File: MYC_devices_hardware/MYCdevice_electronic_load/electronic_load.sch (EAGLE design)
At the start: 129 parts, among them IC1 MEGA16-P, IC10 Gate7, IC11 LF347N, IC12 LF347N, IC14 MCP603CH, IC15 MCP603CH, IC16 MCP603CH, IC17 MCP603CH, IC18 MCP603CH, IC19 MCP603CH, IC2 MAX232, IC20 MCP603CH, IC3 7805TV, IC4 Gate1, IC5 Gate2, IC6 Gate3, IC7 Gate4, IC8 Gate5, IC9 Gate6, Q1 20MHz, X1 8-15V, X2 1503_09, X3 1503_09, X4 RS232

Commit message: deleted duplicate MYCdevice_electronic_load
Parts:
- removed C29, C30, C31, C32, C33: 22uF 1210, rcl:C-EUC1206
- removed R52, R57: 27k, resistor:R-EU_0207/2V
- removed R53, R58: 1k 1%, resistor:R-EU_0207/2V
- removed R54: 9k53, resistor:R-EU_0207/2V
- removed R55, R60: 22k, resistor:R-EU_0207/2V
- removed R56: 9k1 1%, resistor:R-EU_0207/2V
- removed R59: 9k52, resistor:R-EU_0207/2V
- removed SL7: U/Iin, con-amp-quick:M05
- added IC13: 78L5, v-reg:78LXX
- added R18, R20: 154k, resistor:R-EU_0207/2V
- added R19, R21: 18k, resistor:R-EU_0207/2V
- added T1: BC807, transistor:BC807-16-PNP-SOT23-BEC
- added T2: BC817, transistor:BC817-16-NPN-SOT23-BEC
- C10, C9: value 22u 1210 -> 22uF 1210
- C11, C12, C13, C14, C15, C16, C17, C18, C19, C20, C21, C22, C23, C24, C25: value 22u -> 22uF 1210; device resistor:C-EUC1206 -> rcl:C-EUC1206
- C2, C3: value 22uF 1210 -> 18pF; device rcl:C-EUC1206 -> resistor:C-EU025-025X050
- C28: value 22uF 1210 -> 1u; device rcl:C-EUC1206 -> resistor:C-EUC1206
- C4: value 18pF -> 22uF 1210; device resistor:C-EU025-025X050 -> rcl:C-EUC1206
- C5: value 18pF -> 22u 1210; device resistor:C-EU025-025X050 -> rcl:C-EUC1206
- C6: value 22uF 1210 -> 22u 1210
- IC10: value Gate7 -> MCP4921
- IC11, IC12: value LF347N -> LM324N; device linear:LF347N -> linear:LM324N
- IC3: value 7805TV -> 79L09; device linear:7805TV -> v-reg:78LXX
- IC4: value Gate1 -> MCP4921
- IC5: value Gate2 -> MCP4921
- IC6: value Gate3 -> MCP4921
- IC7: value Gate4 -> MCP4921
- IC8: value Gate5 -> MCP4921
- IC9: value Gate6 -> MCP4921
- L1: value (none) -> 22u
- R10, R12, R14, R16, R4, R6, R8: value 10k -> 12k
- R11, R13, R15, R17, R5, R7, R9: value 10k -> 8k2
- R22: value 68k 1% -> 154k
- R23: value na -> 18k
- R24: value 9k1 1% -> 154k
- R25: value 27k -> 18k
- R26, R38, R48: value 1k 1% -> 154k
- R27, R39, R49: value 9k53 -> 18k
- R28: value 1,8 1% -> 1k5; device resistor:R-EU_0207/2V -> resistor:R-EU_R1206
- R29: value 220k -> 180; device resistor:R-EU_0207/2V -> resistor:R-EU_R1206
- R30, R40, R50: value 22k -> 154k
- R31, R41, R46, R51: value 9k1 1% -> 18k
- R32, R42, R47: value 27k -> 154k
- R33, R43: value 1k 1% -> 18k
- R34: value 9k53 -> 8k2; device resistor:R-EU_0207/2V -> resistor:R-EU_R1206
- R35: value 22k -> 18k; device resistor:R-EU_0207/2V -> resistor:R-EU_R1206
- R36: value 9k1 1% -> 10k; device resistor:R-EU_0207/2V -> resistor:R-EU_R1206
- R37: value 27k -> 10k; device resistor:R-EU_0207/2V -> resistor:R-EU_R1206
- R44: value 9k53 -> 154k
- R45: value 22k -> 18k
- SL1: value Gates -> Gates1
- SL2: value Gates -> Gates2
- SL4, SL5: value U/Iin -> Iin
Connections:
- net N$29 renamed FET5
- removed net N$57 (its old number): C25.1, R53.2, R54.2, SL7.1
- removed net N$75: IC15.+IN, R35.1
- removed net N$77: IC16.-IN, R36.2, R37.2, R38.1, R39.1
- removed net N$78: C17.1, R40.2, SL5.3
- removed net N$83: IC11A.+IN, IC4A.VOUT
- removed net N$84: IC19.-IN, R51.2, R52.2, R53.1, R54.1
- removed net N$85: IC19.+IN, R55.1
- removed net N$86: C24.1, R55.2, SL7.2
- removed net N$87: IC20.-IN, R56.2, R57.2, R58.1, R59.1
- removed net N$88: C22.1, R60.2, SL7.4
- removed net N$92: IC11A.OUT, R4.2, SL1.1
- removed net N$93: IC10A.VOUT, IC12D.+IN
- removed net N$94: IC12D.-IN, R16.1, R17.1
- removed net N$95: IC12D.OUT, R16.2, SL2.3
- new net 9V: C27.1, IC13.IN, IC3.OUT, R34.1
- new net FET1: IC12C.OUT, R16.2, SL2.3
- new net FET2: IC12A.OUT, R12.2, SL2.2
- new net FET3: IC12D.OUT, R14.2, SL2.1
- new net FET4: IC11B.OUT, R6.2, SL1.4
- new net FET6: IC11A.OUT, R4.2, SL1.2
- new net FET7: IC11D.OUT, R10.2, SL1.1
- new net GON: IC1.(OC1A)PD5, R36.1
- new net N$27: R29.2, SL6.5
- new net N$29: R21.2, SL4.4
- new net N$32: IC20.-IN, R32.1, R33.1
- new net N$39: IC10A.VOUT, R17.2
- new net N$41: IC16.-IN, R22.1, R23.1
- new net N$45: IC17.-IN, R24.1, R25.1
- new net N$52: R48.1, SL6.1
- new net N$53: R31.2, SL6.2
- new net N$55: IC5A.VOUT, R7.2
- new net N$64: R36.2, T2.B
- new net N$65: R38.1, SL4.1
- new net N$72: IC18.+IN, R46.1, R47.2
- new net VREF: IC11A.+IN, IC11B.+IN, IC11C.+IN, IC11D.+IN, IC12A.+IN, IC12C.+IN, IC12D.+IN, R34.2, R35.1
- net C13: now also C5.1; no longer C7.1
- net GND: now also C1.1, C10.2, C2.1, C4.2, C8.1, C9.2, IC12B.+IN, IC13.GND, IC14.!CS, IC15.!CS, IC16.!CS, IC17.!CS, IC18.!CS, IC19.!CS, IC20.!CS, R35.2, R39.2, R41.2, R43.2, R45.2, R46.2, R49.2, R51.2, SL2.4, T2.E, X4.5; no longer C1.2, C10.1, C2.2, C29.2, C30.2, C31.2, C32.2, C33.2, C4.1, C5.1, C6.2, IC12C.-IN, R11.2, R13.2, R15.2, R17.2, R29.2, R5.2, R7.2, R9.2, SL4.5, SL5.5, SL6.5, SL7.5
- net I1: now also IC1.(ADC1)PA1, R18.2; no longer IC1.(ADC6)PA6, R24.1, R25.1
- net I2: now also IC1.(ADC2)PA2, R20.2; no longer IC1.(ADC5)PA5, R31.1, R32.1
- net I3: now also IC1.(ADC3)PA3, R22.2; no longer IC1.(ADC4)PA4, R36.1, R37.1
- net I4: now also IC1.(ADC4)PA4, R24.2; no longer IC1.(ADC3)PA3, R41.1, R42.1
- net I5: now also IC1.(ADC5)PA5, R26.2; no longer IC1.(ADC2)PA2, R46.1, R47.1
- net I6: now also IC1.(ADC6)PA6, R30.2; no longer IC1.(ADC1)PA1, R51.1, R52.1
- net I7: now also IC1.(ADC7)PA7, R32.2; no longer IC1.(ADC0)PA0, R56.1, R57.1
- net N$1: now also IC14.-IN, R18.1, R19.1; no longer C2.1, IC3.VO, JP7.4, L1.1
- net N$10: now also R9.2; no longer IC11C.+IN
- net N$12: now also D1.A, L1.2; no longer IC11D.OUT, R10.2, SL1.4
- net N$13: now also C6.1; no longer C8.1
- net N$14: now also C5.2; no longer C7.2
- net N$16: now also C7.1; no longer C9.1
- net N$17: now also C8.2; no longer C10.2
- net N$19: now also C2.2; no longer C4.2
- net N$21: now also R11.2; no longer IC11D.+IN
- net N$24: now also R13.2; no longer IC12A.+IN
- net N$25: now also C4.1; no longer C6.1
- net N$26: now also R15.2; no longer IC12B.+IN
- net N$3: now also C6.2; no longer C8.2
- net N$30: now also IC15.-IN, R20.1, R21.1; no longer IC12A.OUT, R12.2, SL2.1
- net N$31: now also IC4A.VOUT, R5.2; no longer IC12B.OUT, R14.2, SL2.2
- net N$34: now also IC19.-IN, R30.1, R31.1; no longer C11.1, R45.2, SL6.1
- net N$35: now also C1.2; no longer C3.2
- net N$37: now also C3.2; no longer C5.2
- net N$40: now also IC12D.-IN; no longer IC12B.-IN
- net N$44: now also IC17.+IN, R45.1; no longer C16.1, R43.2, SL5.4
- net N$47: now also IC18.-IN, R26.1, R27.1; no longer C19.1, R35.2, SL5.1
- net N$48: now also R47.1, SL5.4; no longer IC17.-IN, R41.2, R42.2, R43.1, R44.1
- net N$49: now also IC15.+IN, R40.2, R41.1; no longer C12.1, R33.2, R34.2, SL4.4
- net N$54: now also R25.2, SL5.3; no longer IC17.+IN, R45.1
- net N$56: now also C26.1, IC3.IN, T1.E; no longer C1.1, IC11P.V+, IC12P.V+, IC3.VI
- net N$58: now also IC12C.-IN, R16.1, R17.1; no longer IC18.-IN, R46.2, R47.2, R48.1, R49.1
- net N$59: now also C24.1, C25.1, IC11P.V+, IC12P.V+, T1.C; no longer C20.1, R50.2, SL6.4
- net N$60: now also R27.2, SL5.5; no longer IC18.+IN, R50.1
- net N$61: now also R37.2, T1.B; no longer C21.1, R48.2, R49.2, SL6.3
- net N$63: now also R37.1, T2.C; no longer IC11B.+IN, IC5A.VOUT
- net N$66: now also R40.1, SL4.3; no longer C15.1, R22.2, R23.2, SL4.1
- net N$67: now also IC14.+IN, R38.2, R39.1; no longer IC14.-IN, R24.2, R25.2, R26.1, R27.1
- net N$68: now also R42.2, SL4.5; no longer C13.1, R30.2, SL4.3
- net N$69: now also R19.2, SL4.2; no longer IC14.+IN, R30.1
- net N$7: now also L1.1; no longer D1.A
- net N$70: now also R44.1, SL5.2; no longer C14.1, R26.2, R27.2, SL4.2
- net N$74: now also IC19.+IN, R48.2, R49.1; no longer IC15.-IN, R31.2, R32.2, R33.1, R34.1
- net N$76: now also R50.1, SL6.3; no longer IC11B.OUT, R6.2, SL1.2
- net N$79: now also R23.2, SL5.1; no longer IC16.+IN, R40.1
- net N$80: now also IC16.+IN, R42.1, R43.1; no longer C18.1, R38.2, R39.2, SL5.2
- net N$89: now also R33.2, SL6.4; no longer IC20.+IN, R60.1
- net N$90: now also IC20.+IN, R50.2, R51.1; no longer C23.1, R58.2, R59.2, SL7.3
- net N$96: now also IC12B.-IN, IC12B.OUT; no longer IC12C.+IN, IC12C.OUT
- net U: now also C28.1, IC1.(ADC0)PA0; no longer IC1.(ADC7)PA7, R22.1, R23.1
- net VDD: now also C10.1, C11.1, C12.1, C13.1, C14.1, C15.1, C16.1, C17.1, C18.1, C19.1, C20.1, C21.1, C22.1, C23.1, C7.2, C9.1, IC13.OUT, JP7.4; no longer C26.1, C27.1, C28.1, C29.1, C30.1, C31.1, C32.1, C33.1, C9.2, L1.2
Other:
- note added: "+ extern 51k for 90V"
- moved on the sheet: C1, C10, C2, C26, C27, C3, C4, C5, C6, C7, C8, C9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

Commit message: new Hardware for electronic load, firmware and description adapted
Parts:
- removed JP1: Power, jumper:JP1E
- IC14, IC15, IC16, IC17, IC18, IC19, IC20: value MCP603CH -> MCP6031
- R34: value 8k2 -> 1k3
- R35: value 18k -> 1k
- R38, R40, R42, R44, R47, R48, R50: value 154k -> 18k
- R39, R43, R45, R46, R49, R51: value 18k -> 154k
- R41: value 18k -> 154
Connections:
- net N$11 renamed LDAC
- net N$23 renamed S6
- net N$4 renamed S7
- net N$50 renamed S2
- net N$51 renamed S1
- net N$62 renamed S4
- net N$71 renamed S3
- net N$8 renamed S5
- removed net N$25: C4.1, IC1.AVCC, IC1.VCC, JP1.1, JP6.2
- net FET1: now also IC11D.OUT, R10.2, SL1.1; no longer IC12C.OUT, R16.2, SL2.3
- net FET2: now also IC11A.OUT, R4.2, SL1.2; no longer IC12A.OUT, R12.2, SL2.2
- net FET3: now also IC11C.OUT, R8.2, SL1.3; no longer IC12D.OUT, R14.2, SL2.1
- net FET5: now also IC12D.OUT, R14.2, SL2.1; no longer IC11C.OUT, R8.2, SL1.3
- net FET6: now also IC12A.OUT, R12.2, SL2.2; no longer IC11A.OUT, R4.2, SL1.2
- net FET7: now also IC12C.OUT, R16.2, SL2.3; no longer IC11D.OUT, R10.2, SL1.1
- net VDD: now also C4.1, IC1.AVCC, IC1.VCC, JP6.2; no longer JP1.2

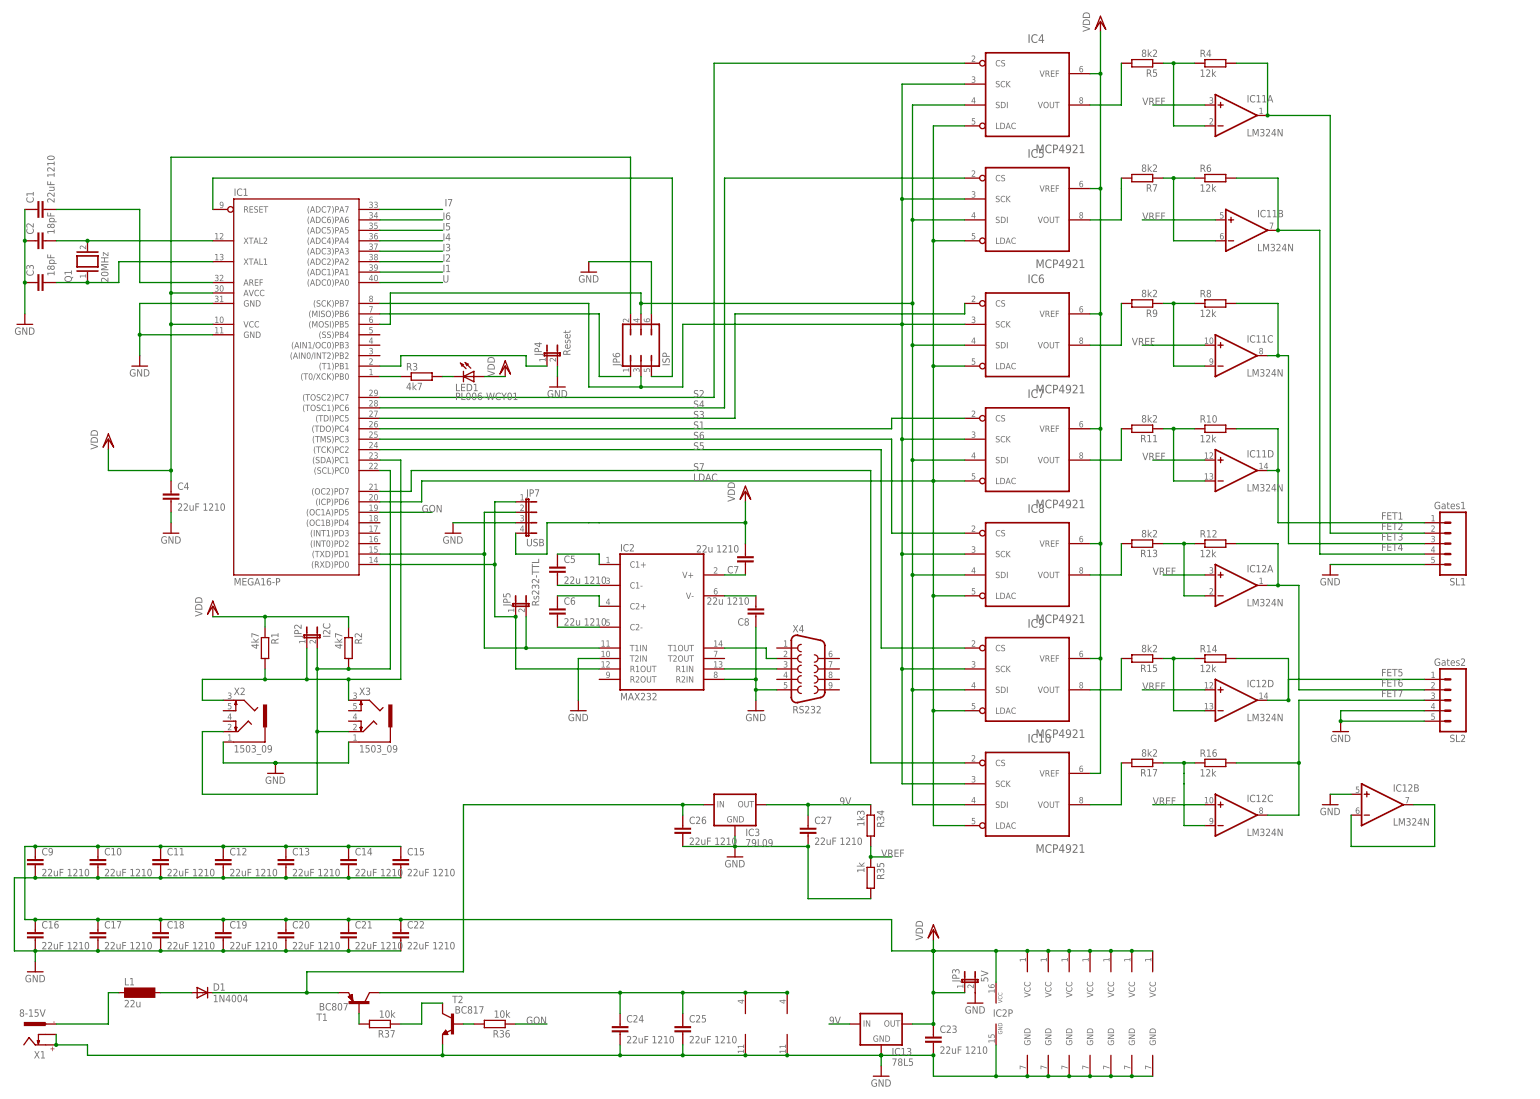
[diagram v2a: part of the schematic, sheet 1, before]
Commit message: board: 3V I2c, bascom: include files used
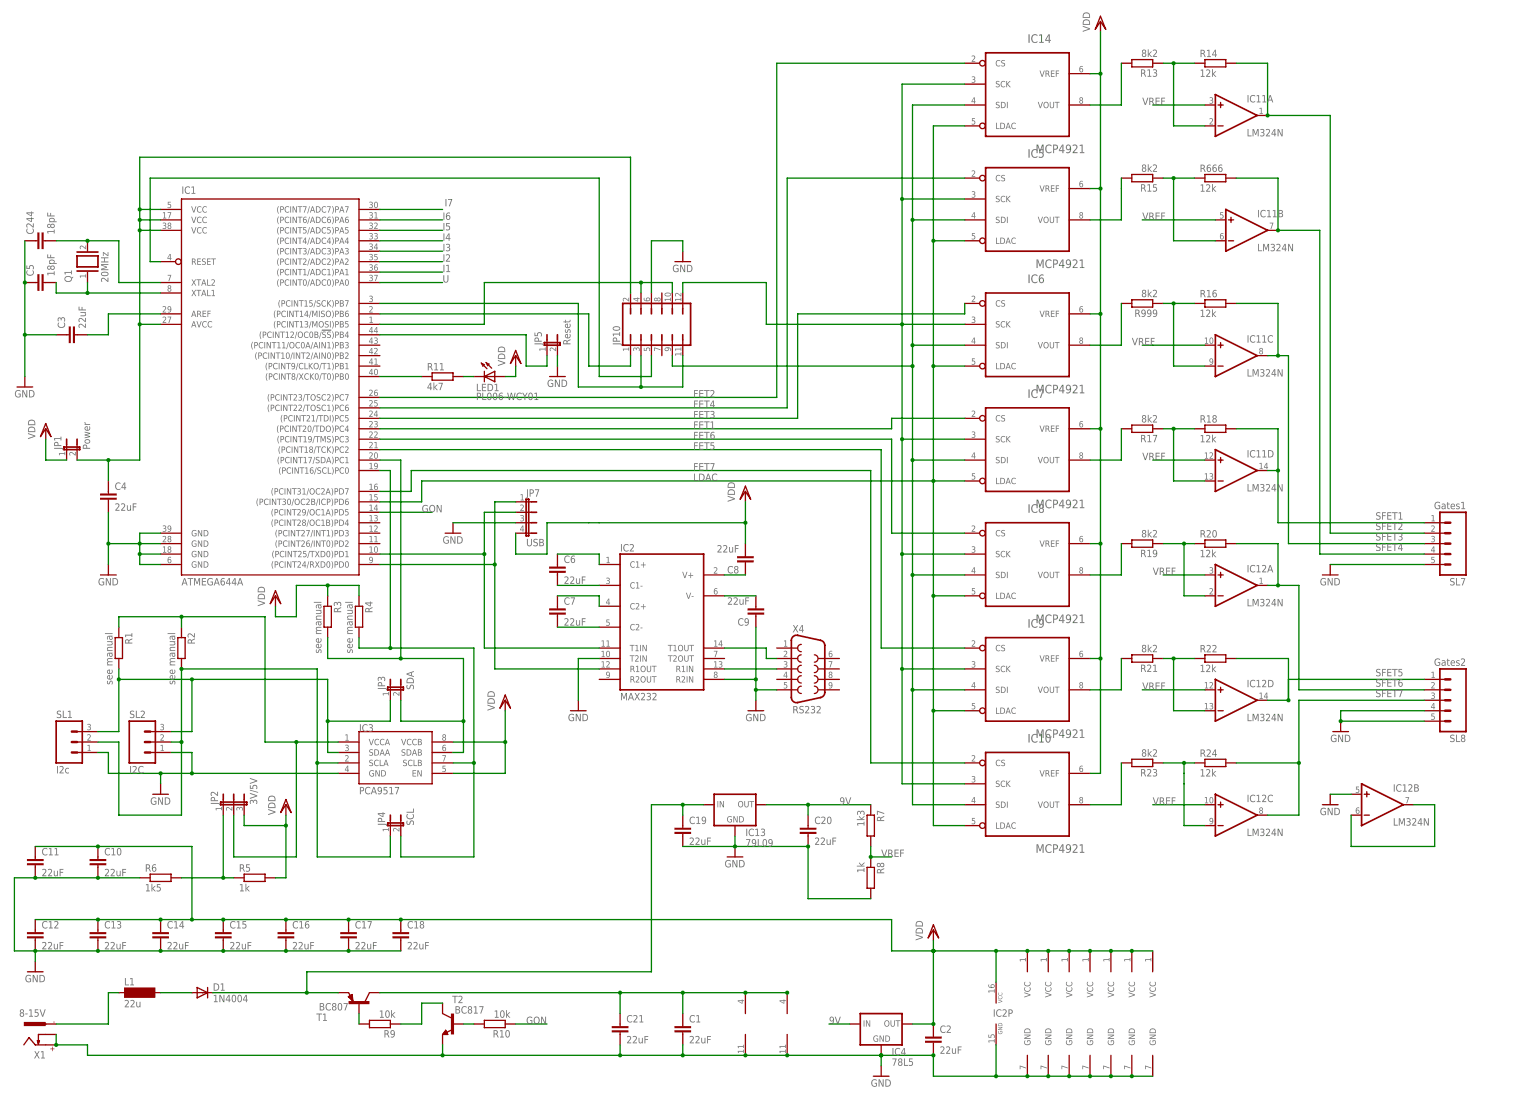
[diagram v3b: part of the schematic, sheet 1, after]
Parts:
- removed C23, C24, C25, C26, C27: 22uF 1210, rcl:C-EUC1206
- removed C28: 1u, resistor:C-EUC1206
- removed IC15, IC16, IC17, IC18, IC19, IC20: MCP6031, linear:MCP603CH
- removed JP6: ISP, jumper:JP3Q
- removed R12: 12k, resistor:R-EU_R1206
- removed X2, X3: 1503_09, con-lumberg:1503_09
- added C244: 18pF, resistor:C-EU025-025X050
- added IC21, IC22: MCP60x4, linear:LM324D
- added JP1: Power, jumper:JP1E
- added JP10: (no value), jumper:JP6Q
- added JP11, JP12: (no value), jumper:JP4E
- added R52: 18k, resistor:R-EU_M1206
- added R53: 180, resistor:R-EU_R1206
- added R54: 1k5, resistor:R-EU_R1206
- added R666: 12k, resistor:R-EU_R1206
- added R999: 8k2, resistor:R-EU_R1206
- added SL7: Gates1, con-amp-quick:M05
- added SL8: Gates2, con-amp-quick:M05
- C1, C10, C11, C12, C13, C14, C15, C16, C17, C18, C19, C20, C21, C4, C9: value 22uF 1210 -> 22uF
- C2, C3: value 18pF -> 22uF; device resistor:C-EU025-025X050 -> rcl:C-EUC1206
- C22: value 22uF 1210 -> 1u; device rcl:C-EUC1206 -> resistor:C-EUC1206
- C5: value 22u 1210 -> 18pF; device rcl:C-EUC1206 -> resistor:C-EU025-025X050
- C6, C7, C8: value 22u 1210 -> 22uF
- IC1: value MEGA16-P -> ATMEGA644A; device atmel:MEGA16-P -> atmel:ATMEGA644A
- IC13: value 78L5 -> 79L09
- IC14: value MCP6031 -> MCP4921; device linear:MCP603CH -> dac:MCP491
- IC3: value 79L09 -> PCA9517; device v-reg:78LXX -> PCA9517:PCA9517
- IC4: value MCP4921 -> 78L5; device dac:MCP491 -> v-reg:78LXX
- JP2: value I2C -> 3V/5V; device jumper:JP1E -> jumper:JP2E
- JP3: value 5V -> SDA
- JP4: value Reset -> SCL
- JP5: value Rs232-TTL -> Reset
- R1, R2: value 4k7 -> see manual; device resistor:R-EU_0207/2V -> resistor:R-EU_R1206
- R10: value 12k -> 10k
- R11: value 8k2 -> 4k7
- R18, R20, R22, R24: value 154k -> 12k; device resistor:R-EU_0207/2V -> resistor:R-EU_R1206
- R19, R21, R23: value 18k -> 8k2; device resistor:R-EU_0207/2V -> resistor:R-EU_R1206
- R25, R27, R33, R47: value 18k -> 154k; device resistor:R-EU_0207/2V -> resistor:R-EU_M1206
- R26, R30, R32, R46: value 154k -> 18k; device resistor:R-EU_0207/2V -> resistor:R-EU_M1206
- R28: value 1k5 -> 18k
- R29: value 180 -> 154k; device resistor:R-EU_R1206 -> resistor:R-EU_M1206
- R3: value 4k7 -> see manual
- R31: value 18k -> 154; device resistor:R-EU_0207/2V -> resistor:R-EU_M1206
- R34: value 1k3 -> 18k; device resistor:R-EU_R1206 -> resistor:R-EU_M1206
- R35: value 1k -> 154k; device resistor:R-EU_R1206 -> resistor:R-EU_M1206
- R36: value 10k -> 18k; device resistor:R-EU_R1206 -> resistor:R-EU_M1206
- R37: value 10k -> 154k; device resistor:R-EU_R1206 -> resistor:R-EU_M1206
- R38, R39, R40, R42, R43, R44, R45, R48, R49, R50, R51: device resistor:R-EU_0207/2V -> resistor:R-EU_M1206
- R4: value 12k -> see manual
- R41: value 154 -> 154k; device resistor:R-EU_0207/2V -> resistor:R-EU_M1206
- R5: value 8k2 -> 1k
- R6: value 12k -> 1k5
- R7: value 8k2 -> 1k3
- R8: value 12k -> 1k
- R9: value 8k2 -> 10k
- SL1: value Gates1 -> I2c; device con-amp-quick:M05 -> con-amp-quick:M03
- SL2: value Gates2 -> I2C; device con-amp-quick:M05 -> con-amp-quick:M03
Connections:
- removed net S1: IC1.(TDO)PC4, IC7A.CS
- removed net S2: IC1.(TOSC2)PC7, IC4A.CS
- removed net S3: IC1.(TDI)PC5, IC6A.CS
- removed net S4: IC1.(TOSC1)PC6, IC5A.CS
- removed net S5: IC1.(TCK)PC2, IC9A.CS
- removed net S6: IC1.(TMS)PC3, IC8A.CS
- removed net S7: IC1.(OC2)PD7, IC10A.CS
- new net N$11: C5.2, IC1.XTAL1, Q1.1
- new net N$23: IC1.(PCINT13/MOSI)PB5, JP10.10, JP10.4
- new net N$25: C3.2, IC1.AREF
- new net N$4: C4.1, IC1.AVCC, IC1.VCC, IC1.VCC@1, IC1.VCC@2, JP1.2, JP10.2
- new net N$50: IC1.(PCINT16/SCL)PC0, IC3.SCLB, JP4.2, R4.2
- new net N$51: JP2.1, R5.1, R6.2
- new net N$62: IC3.VCCA, JP2.2, R1.1, R2.1
- new net N$8: IC22B.-IN, IC22B.OUT
- new net SFET1: IC11D.OUT, R18.2, SL7.1
- new net SFET2: IC11A.OUT, R14.2, SL7.2
- new net SFET3: IC11C.OUT, R16.2, SL7.3
- new net SFET4: IC11B.OUT, R666.2, SL7.4
- new net SFET5: IC12D.OUT, R22.2, SL8.1
- new net SFET6: IC12A.OUT, R20.2, SL8.2
- new net SFET7: IC12C.OUT, R24.2, SL8.3
- net 9V: now also C20.1, IC13.OUT, IC4.IN, R7.1; no longer C27.1, IC13.IN, IC3.OUT, R34.1
- net C13: now also C6.1; no longer C5.1
- net FET1: now also IC1.(PCINT20/TDO)PC4, IC7A.CS; no longer IC11D.OUT, R10.2, SL1.1
- net FET2: now also IC1.(PCINT23/TOSC2)PC7, IC14A.CS; no longer IC11A.OUT, R4.2, SL1.2
- net FET3: now also IC1.(PCINT21/TDI)PC5, IC6A.CS; no longer IC11C.OUT, R8.2, SL1.3
- net FET4: now also IC1.(PCINT22/TOSC1)PC6, IC5A.CS; no longer IC11B.OUT, R6.2, SL1.4
- net FET5: now also IC1.(PCINT18/TCK)PC2, IC9A.CS; no longer IC12D.OUT, R14.2, SL2.1
- net FET6: now also IC1.(PCINT19/TMS)PC3, IC8A.CS; no longer IC12A.OUT, R12.2, SL2.2
- net FET7: now also IC1.(PCINT31/OC2A)PD7, IC10A.CS; no longer IC12C.OUT, R16.2, SL2.3
- net GND: now also C1.2, C2.2, C244.1, C5.1, C9.1, IC1.GND@2, IC1.GND@3, IC14P.GND, IC21P.V-, IC22B.+IN, IC22P.V-, IC4.GND, JP10.6, JP5.2, R27.2, R31.2, R47.2, R54.2, R6.1, R8.2, SL1.1, SL2.1, SL7.5, SL8.4, SL8.5; no longer C1.1, C2.1, C23.2, C24.2, C25.2, C26.2, C27.2, C28.2, C8.1, C9.2, IC14.!CS, IC14.V-, IC15.!CS, IC15.V-, IC16.!CS, IC16.V-, IC17.!CS, IC17.V-, IC18.!CS, IC18.V-, IC19.!CS, IC19.V-, IC20.!CS, IC20.V-, IC4P.GND, JP3.2, JP4.2, JP6.6, R28.2, R41.2, R45.2, R46.2, R49.2, SL1.5, SL2.4, SL2.5, X2.1, X3.1
- net GON: now also IC1.(PCINT29/OC1A)PD5, R10.1; no longer IC1.(OC1A)PD5, R36.1
- net I1: now also IC1.(PCINT1/ADC1)PA1, IC21A.OUT, JP12.1, R25.2; no longer IC1.(ADC1)PA1, IC14.OUT, R18.2
- net I2: now also IC1.(PCINT2/ADC2)PA2, IC21B.OUT, JP12.2, R29.2; no longer IC1.(ADC2)PA2, IC15.OUT, R20.2
- net I3: now also IC1.(PCINT3/ADC3)PA3, IC21D.OUT, JP12.3, R33.2; no longer IC1.(ADC3)PA3, IC16.OUT, R22.2
- net I4: now also IC1.(PCINT4/ADC4)PA4, IC21C.OUT, JP12.4, R37.2; no longer IC1.(ADC4)PA4, IC17.OUT, R24.2
- net I5: now also IC1.(PCINT5/ADC5)PA5, IC22A.OUT, JP11.1, R41.2; no longer IC1.(ADC5)PA5, IC18.OUT, R26.2
- net I6: now also IC1.(PCINT6/ADC6)PA6, IC22D.OUT, JP11.2, R45.2; no longer IC1.(ADC6)PA6, IC19.OUT, R30.2
- net I7: now also IC1.(PCINT7/ADC7)PA7, IC22C.OUT, JP11.3, R49.2; no longer IC1.(ADC7)PA7, IC20.OUT, R32.2
- net LDAC: now also IC1.(PCINT30/OC2B/ICP)PD6, IC14A.LDAC; no longer IC1.(ICP)PD6, IC4A.LDAC
- net N$1: now also IC21A.-IN, R25.1, R26.1; no longer IC14.-IN, R18.1, R19.1
- net N$10: now also R999.2; no longer R9.2
- net N$13: now also C7.1; no longer C6.1
- net N$14: now also C6.2; no longer C5.2
- net N$15: now also IC1.(PCINT14/MISO)PB6, JP10.1; no longer IC1.(MISO)PB6, JP6.1
- net N$16: now also C8.1; no longer C7.1
- net N$17: now also C9.2; no longer C8.2
- net N$18: now also JP10.5; no longer JP6.5
- net N$19: now also C244.2; no longer C2.2
- net N$2: now also IC1.(PCINT24/RXD0)PD0; no longer IC1.(RXD)PD0, JP5.1
- net N$20: now also IC14A.SDI, JP10.9; no longer IC1.(MOSI)PB5, IC4A.SDI, JP6.4
- net N$21: now also R17.2; no longer R11.2
- net N$22: now also IC3.SCLA, JP4.1, SL1.2, SL2.2; no longer IC1.(SCL)PC0, JP2.2, X2.2, X3.2
- net N$24: now also R19.2; no longer R13.2
- net N$26: now also R21.2; no longer R15.2
- net N$27: now also R53.2; no longer R29.2
- net N$28: now also IC14A.SCK, JP10.12; no longer IC1.(SCK)PB7, IC4A.SCK, JP6.3
- net N$29: now also R30.2; no longer R21.2
- net N$3: now also C7.2; no longer C6.2
- net N$30: now also IC21B.-IN, R29.1, R30.1; no longer IC15.-IN, R20.1, R21.1
- net N$31: now also IC14A.VOUT, R13.2; no longer IC4A.VOUT, R5.2
- net N$32: now also IC22C.-IN, R49.1, R50.1; no longer IC20.-IN, R32.1, R33.1
- net N$34: now also IC22D.-IN, R45.1, R46.1; no longer IC19.-IN, R30.1, R31.1
- net N$35: now also IC1.(PCINT17/SDA)PC1, IC3.SDAB, JP3.2, R3.2; no longer C1.2, IC1.AREF
- net N$36: now also R17.1, R18.1; no longer R10.1, R11.1
- net N$37: now also IC1.(PCINT12/OC0B/!SS!)PB4, JP5.1; no longer C3.2, IC1.XTAL1, Q1.1
- net N$38: now also R16.1, R999.1; no longer R8.1, R9.1
- net N$39: now also R23.2; no longer R17.2
- net N$40: now also R21.1, R22.1; no longer R14.1, R15.1
- net N$41: now also IC21D.-IN, R33.1, R34.1; no longer IC16.-IN, R22.1, R23.1
- net N$42: now also IC1.(PCINT8/XCK0/T0)PB0, R11.1; no longer IC1.(T0/XCK)PB0, R3.1
- net N$43: now also R11.2; no longer R3.2
- net N$44: now also IC21C.+IN, R39.1, R40.2; no longer IC17.+IN, R44.2, R45.1
- net N$45: now also IC21C.-IN, R37.1, R38.1; no longer IC17.-IN, R24.1, R25.1
- net N$46: now also IC1.(PCINT15/SCK)PB7, JP10.11, JP10.3; no longer IC1.(T1)PB1, JP4.1
- net N$47: now also IC22A.-IN, R41.1, R42.1; no longer IC18.-IN, R26.1, R27.1
- net N$48: now also R44.1; no longer R47.1
- net N$49: now also IC21B.+IN, R31.1, R32.2; no longer IC15.+IN, R40.2, R41.1
- net N$5: now also IC3.SDAA, JP3.1, SL1.3, SL2.3; no longer IC1.(SDA)PC1, JP2.1, X2.3, X3.3
- net N$53: now also R46.2; no longer R31.2
- net N$54: now also R38.2; no longer R25.2
- net N$55: now also R15.2; no longer R7.2
- net N$56: now also C19.1, IC13.IN; no longer C26.1, IC3.IN
- net N$57: now also R19.1, R20.1; no longer R12.1, R13.1
- net N$58: now also R23.1, R24.1; no longer R16.1, R17.1
- net N$59: now also C1.1, C21.1; no longer C24.1, C25.1
- net N$6: now also IC1.(PCINT25/TXD0)PD1; no longer IC1.(TXD)PD1, JP5.2
- net N$60: now also R42.2; no longer R27.2
- net N$61: now also R9.2; no longer R37.2
- net N$63: now also R9.1; no longer R37.1
- net N$64: now also R10.2; no longer R36.2
- net N$65: now also R28.1; no longer R38.1
- net N$66: now also R32.1; no longer R40.1
- net N$67: now also IC21A.+IN, R27.1, R28.2; no longer IC14.+IN, R38.2, R39.1
- net N$68: now also R36.2; no longer R42.2
- net N$69: now also R26.2; no longer R19.2
- net N$70: now also R40.1; no longer R44.1
- net N$72: now also IC22A.+IN, R43.1, R44.2; no longer IC18.+IN, R46.1, R47.2
- net N$73: now also R15.1, R666.1; no longer R6.1, R7.1
- net N$74: now also IC22D.+IN, R47.1; no longer IC19.+IN, R49.1
- net N$76: now also R52.1; no longer R50.1
- net N$79: now also R34.2; no longer R23.2
- net N$80: now also IC21D.+IN, R35.1, R36.1; no longer IC16.+IN, R42.1, R43.1
- net N$89: now also R50.2; no longer R33.2
- net N$90: now also IC22C.+IN, R52.2; no longer IC20.+IN, R50.2
- net N$91: now also R13.1, R14.1; no longer R4.1, R5.1
- net U: now also C22.1, IC1.(PCINT0/ADC0)PA0, R53.1, R54.1; no longer C28.1, IC1.(ADC0)PA0, R28.1, R29.1
- net VDD: now also C2.1, C8.2, IC14A.VREF, IC14P.VCC, IC21P.V+, IC22P.V+, IC3.EN, IC3.VCCB, IC4.OUT, JP1.1, JP2.3, R3.1, R4.1, R5.2; no longer C19.1, C20.1, C21.1, C22.1, C23.1, C4.1, C7.2, C9.1, IC1.AVCC, IC1.VCC, IC13.OUT, IC14.V+, IC15.V+, IC16.V+, IC17.V+, IC18.V+, IC19.V+, IC20.V+, IC4A.VREF, IC4P.VCC, JP3.1, JP6.2, R1.1, R2.1
- net VREF: now also R7.2, R8.1; no longer R34.2, R35.1
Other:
- moved on the sheet: C1, C11, C12, C13, C14, C15, C16, C17, C18, C19, C2, C20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
